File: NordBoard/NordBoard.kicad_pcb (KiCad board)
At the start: 2 copper layers, 18 parts, among them SW1 SW_Push, SW10 SW_Push, SW11 SW_Push, SW12 SW_Push, SW13 SW_Push, SW14 SW_Push, SW17 SW_Push, SW18 SW_Push, SW19 SW_Push, SW20 SW_Push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

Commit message: feat: finish schem, finish PCB layout
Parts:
- removed SW1, SW10, SW11, SW12, SW13, SW14, SW17, SW18, SW19, SW20, SW21, SW3, SW4, SW5, SW6, SW7, SW8: SW_Push, PCM_marbastlib-choc:SW_choc_v1_1u
- removed U1: MOUDLE-SEEEDUINO-XIAO, Seeed Studio XIAO Series Library:XIAO-RP2040-DIP
- added D1: D, Diode_SMD:D_SMA-SMB_Universal_Handsoldering, F.Cu at (55.5, 68.0)
- added D19: D, Diode_SMD:D_SMA-SMB_Universal_Handsoldering, F.Cu at (55.0, 93.5)
- added D20: D, Diode_SMD:D_SMA-SMB_Universal_Handsoldering, F.Cu at (53.9, 121.0)
- added D21: D, Diode_SMD:D_SMA-SMB_Universal_Handsoldering, F.Cu at (75.0, 54.5)
- added D22: D, Diode_SMD:D_SMA-SMB_Universal_Handsoldering, F.Cu at (74.9, 79.5)
- added D23: D, Diode_SMD:D_SMA-SMB_Universal_Handsoldering, F.Cu at (75.5, 104.5)
- added D24: D, Diode_SMD:D_SMA-SMB_Universal_Handsoldering, F.Cu at (96.0, 43.5)
- added D25: D, Diode_SMD:D_SMA-SMB_Universal_Handsoldering, F.Cu at (96.0, 69.5)
- added D26: D, Diode_SMD:D_SMA-SMB_Universal_Handsoldering, F.Cu at (96.0, 94.5)
- added D27: D, Diode_SMD:D_SMA-SMB_Universal_Handsoldering, F.Cu at (116.5, 49.5)
- added D28: D, Diode_SMD:D_SMA-SMB_Universal_Handsoldering, F.Cu at (116.5, 74.5)
- added D29: D, Diode_SMD:D_SMA-SMB_Universal_Handsoldering, F.Cu at (116.4, 100.5)
- added D30: D, Diode_SMD:D_SMA-SMB_Universal_Handsoldering, F.Cu at (121.5, 126.5)
- added D31: D, Diode_SMD:D_SMA-SMB_Universal_Handsoldering, F.Cu at (137.0, 55.0)
- added D32: D, Diode_SMD:D_SMA-SMB_Universal_Handsoldering, F.Cu at (137.9, 80.5)
- added D33: D, Diode_SMD:D_SMA-SMB_Universal_Handsoldering, F.Cu at (137.4, 105.5)
- added D34: D, Diode_SMD:D_SMA-SMB_Universal_Handsoldering, F.Cu at (141.9, 131.5)
- added H1: MountingHole, MountingHole:MountingHole_2.2mm_M2, F.Cu at (48.0, 41.5)
- added H2: MountingHole, MountingHole:MountingHole_2.2mm_M2, F.Cu at (67.5, 111.0)
- added H3: MountingHole, MountingHole:MountingHole_2.2mm_M2, F.Cu at (155.0, 111.0)
- added H4: MountingHole, MountingHole:MountingHole_2.2mm_M2, F.Cu at (144.0, 29.0)
- added SW15: SW_Push, PCM_marbastlib-choc:SW_choc_v1_1u, F.Cu at (54.0, 108.0)
- added SW16: SW_Push, PCM_marbastlib-choc:SW_choc_v1_1u, F.Cu at (75.5, 42.0)
- added SW2: SW_Push, PCM_marbastlib-choc:SW_choc_v1_1u, F.Cu at (55.0, 55.5)
- added SW22: SW_Push, PCM_marbastlib-choc:SW_choc_v1_1u, F.Cu at (75.5, 67.0)
- added SW23: SW_Push, PCM_marbastlib-choc:SW_choc_v1_1u, F.Cu at (75.5, 92.0)
- added SW24: SW_Push, PCM_marbastlib-choc:SW_choc_v1_1u, F.Cu at (96.0, 30.5)
- added SW25: SW_Push, PCM_marbastlib-choc:SW_choc_v1_1u, F.Cu at (96.0, 57.0)
- added SW26: SW_Push, PCM_marbastlib-choc:SW_choc_v1_1u, F.Cu at (96.0, 82.0)
- added SW27: SW_Push, PCM_marbastlib-choc:SW_choc_v1_1u, F.Cu at (116.5, 37.0)
- added SW28: SW_Push, PCM_marbastlib-choc:SW_choc_v1_1u, F.Cu at (116.5, 62.0)
- added SW29: SW_Push, PCM_marbastlib-choc:SW_choc_v1_1u, F.Cu at (116.5, 87.5)
- added SW30: SW_Push, PCM_marbastlib-choc:SW_choc_v1_1u, F.Cu at (121.5, 113.5)
- added SW31: SW_Push, PCM_marbastlib-choc:SW_choc_v1_1u, F.Cu at (137.0, 42.0)
- added SW32: SW_Push, PCM_marbastlib-choc:SW_choc_v1_1u, F.Cu at (137.5, 68.0)
- added SW33: SW_Push, PCM_marbastlib-choc:SW_choc_v1_1u, F.Cu at (137.5, 93.0)
- added SW34: SW_Push, PCM_marbastlib-choc:SW_choc_v1_1u, F.Cu at (142.0, 118.5)
- added SW9: SW_Push, PCM_marbastlib-choc:SW_choc_v1_1u, F.Cu at (55.0, 80.5)
- added U2: Seeeduino Xiao rp2040, PCM_marbastlib-xp-promicroish:Xiao_rp2040_ACH, F.Cu at (159.1, 97.0)

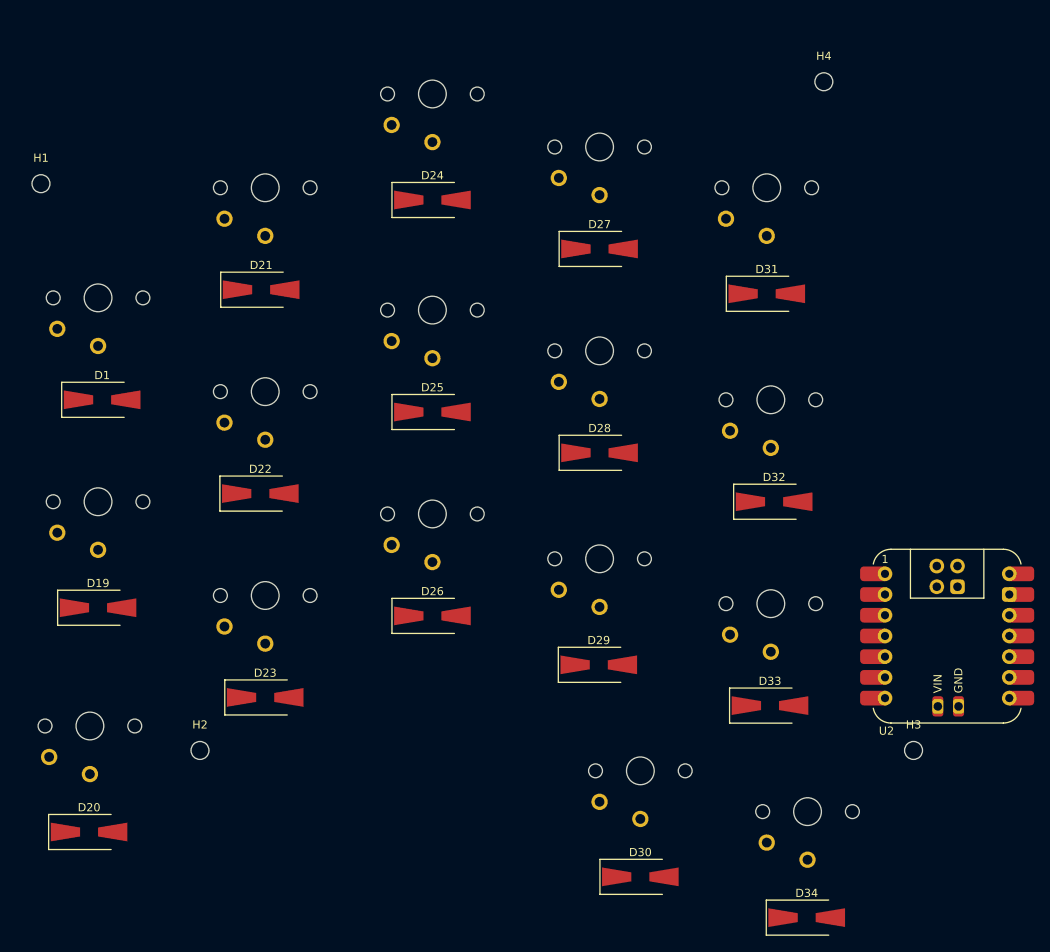
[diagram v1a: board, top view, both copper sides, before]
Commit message: feat: finish pcb layout and cleanup todo routing
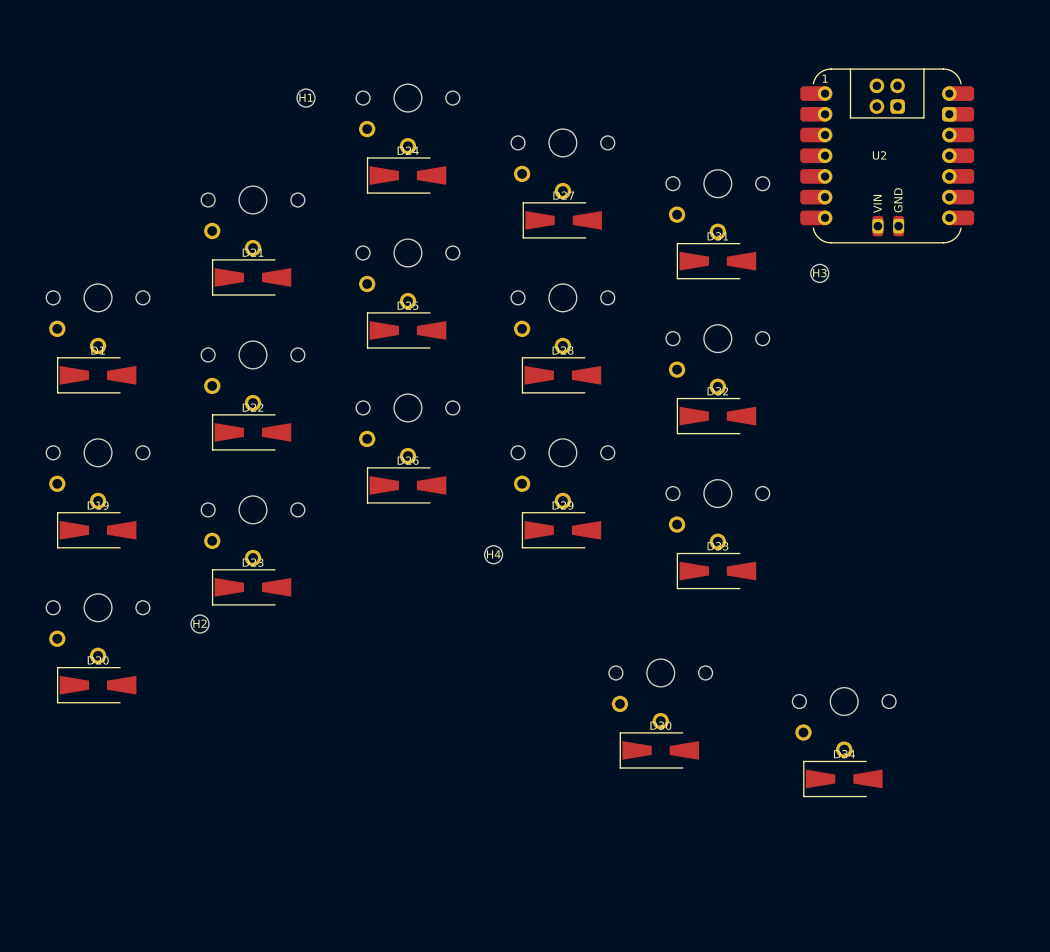
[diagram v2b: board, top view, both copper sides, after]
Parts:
- moved H4 70.7 mm to (103.5, 87.0)
- moved H3 59.6 mm to (143.5, 52.5)
- moved U2 59.3 mm to (151.8, 38.1)
- moved H1 34.2 mm to (80.5, 31.0)
- moved D20 18.0 mm to (55.0, 103.0)
- moved D33 17.7 mm to (131.0, 89.0)
- moved D34 17.6 mm to (146.5, 114.5)
- moved D29 17.1 mm to (112.0, 84.0)
- moved D26 16.3 mm to (93.0, 78.5)
- moved D30 15.7 mm to (124.0, 111.0)
- moved H2 15.5 mm to (67.5, 95.5)
- moved SW33 15.0 mm to (131.0, 79.5)
- moved SW15 14.5 mm to (55.0, 93.5)
- moved SW34 14.2 mm to (146.5, 105.0)
- moved SW29 13.8 mm to (112.0, 74.5)
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
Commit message: feat: finish board routing
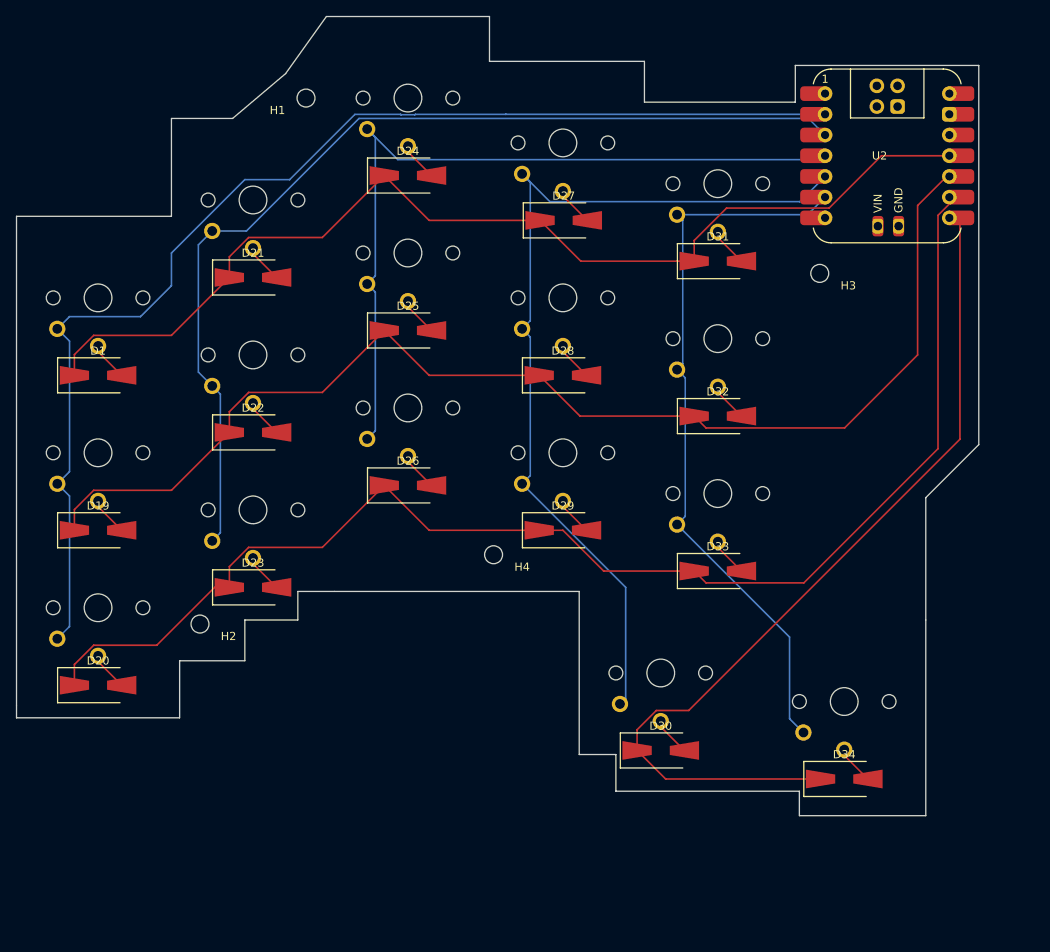
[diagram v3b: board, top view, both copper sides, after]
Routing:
- net /left/ROW2: track 0.00 -> 163.0 mm
- net /left/ROW1: track 0.00 -> 150.2 mm
- net /left/COL0: track 0.00 -> 147.9 mm
- net /left/ROW0: track 0.00 -> 132.9 mm
- net /left/COL1: track 0.00 -> 121.9 mm
- net /left/COL3: track 0.00 -> 112.0 mm
- net /left/ROW3: track 0.00 -> 108.0 mm
- net /left/COL2: track 0.00 -> 97.6 mm
- net /left/COL4: track 0.00 -> 90.4 mm
- net Net-(D27-A): track 0.00 -> 4.84 mm
- net Net-(D31-A): track 0.00 -> 4.80 mm
- net Net-(D28-A): track 0.00 -> 4.80 mm
- net Net-(D25-A): track 0.00 -> 4.80 mm
- net Net-(D24-A): track 0.00 -> 4.80 mm
- net Net-(D21-A): track 0.00 -> 4.80 mm
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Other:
- board outline added: 118 x 98 mm

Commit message: feat: new col in schem (not in PCB)
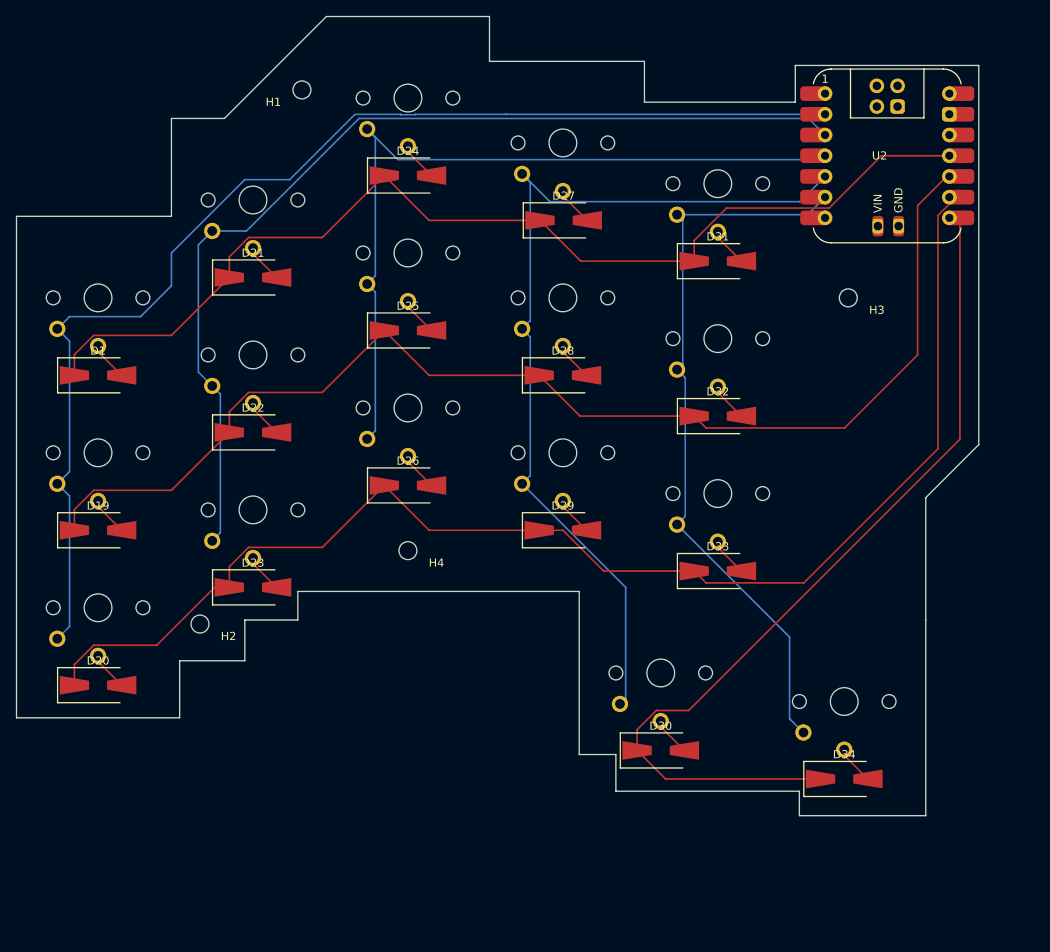
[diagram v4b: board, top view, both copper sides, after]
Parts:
- moved H4 10.5 mm to (93.0, 86.5)
- moved H3 4.61 mm to (147.0, 55.5)
- moved H1 1.12 mm to (80.0, 30.0)
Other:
- outline, holes or cut-outs redrawn
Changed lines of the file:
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@@
 	(footprint "MountingHole:MountingHole_2.2mm_M2"
 		(layer "F.Cu")
-		(at 103.5 87)
+		(at 93 86.5)
 		(descr "Mounting Hole 2.2mm, M2, no annular, generated by kicad-footprint-generator mountinghole.py")
 		(tags "mountinghole M2")
@@
 	(footprint "MountingHole:MountingHole_2.2mm_M2"
 		(layer "F.Cu")
-		(at 80.5 31)
+		(at 80 30)
 		(descr "Mounting Hole 2.2mm, M2, no annular, generated by kicad-footprint-generator mountinghole.py")
 		(tags "mountinghole M2")
@@
 		)
 		(fp_text user "${REFERENCE}"
-			(at 0 0 0)
+			(at 0.5 0 0)
 			(layer "F.Fab")
 			(effects
@@
 	(footprint "MountingHole:MountingHole_2.2mm_M2"
 		(layer "F.Cu")
-		(at 143.5 52.5)
+		(at 147 55.5)
 		(descr "Mounting Hole 2.2mm, M2, no annular, generated by kicad-footprint-generator mountinghole.py")
 		(tags "mountinghole M2")
@@
 		)
 		(fp_text user "${REFERENCE}"
-			(at 0 0 0)
+			(at 0.5 0 0)
 			(layer "F.Fab")
 			(effects
@@
 	)
 	(gr_line
-		(start 71.5 33.5)
-		(end 78 28)
+		(start 70.5 33.5)
+		(end 83 21)
 		(stroke
 			(width 0.05)
@@
 	)
 	(gr_line
-		(start 78 28)
-		(end 83 21)
-		(stroke
-			(width 0.05)
-			(type default)
-		)
-		(layer "Edge.Cuts")
-	)
-	(gr_line
 		(start 45 45.5)
 		(end 64 45.5)
@@
 	(gr_line
 		(start 64 33.5)
-		(end 71.5 33.5)
+		(end 70.5 33.5)
 		(stroke
 			(width 0.05)
